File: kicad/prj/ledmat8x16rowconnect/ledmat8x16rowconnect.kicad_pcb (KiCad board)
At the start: 2 copper layers, 15.9 x 63.8 mm, 2 parts, among them J1 Conn_02x08_Odd_Even, J2 Conn_02x08_Odd_Even

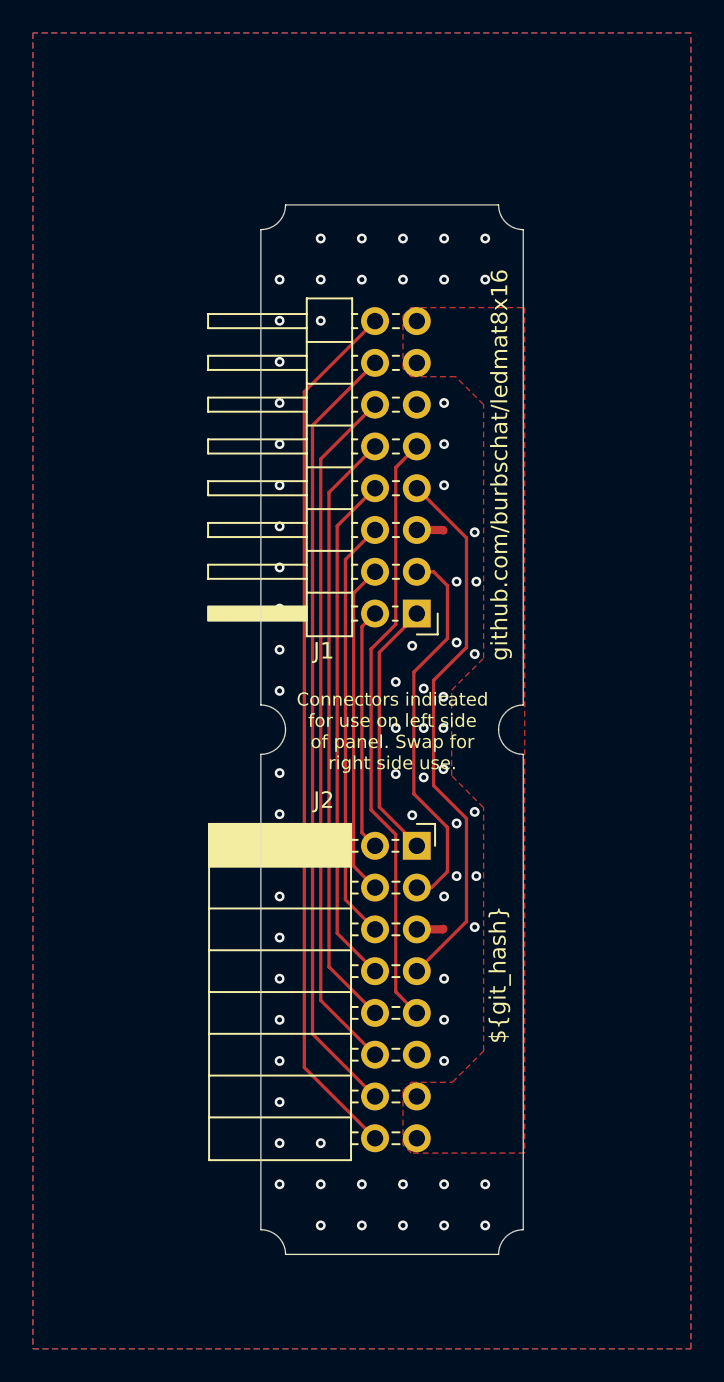
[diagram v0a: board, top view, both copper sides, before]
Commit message: Resize row-connect board to 32mm outline
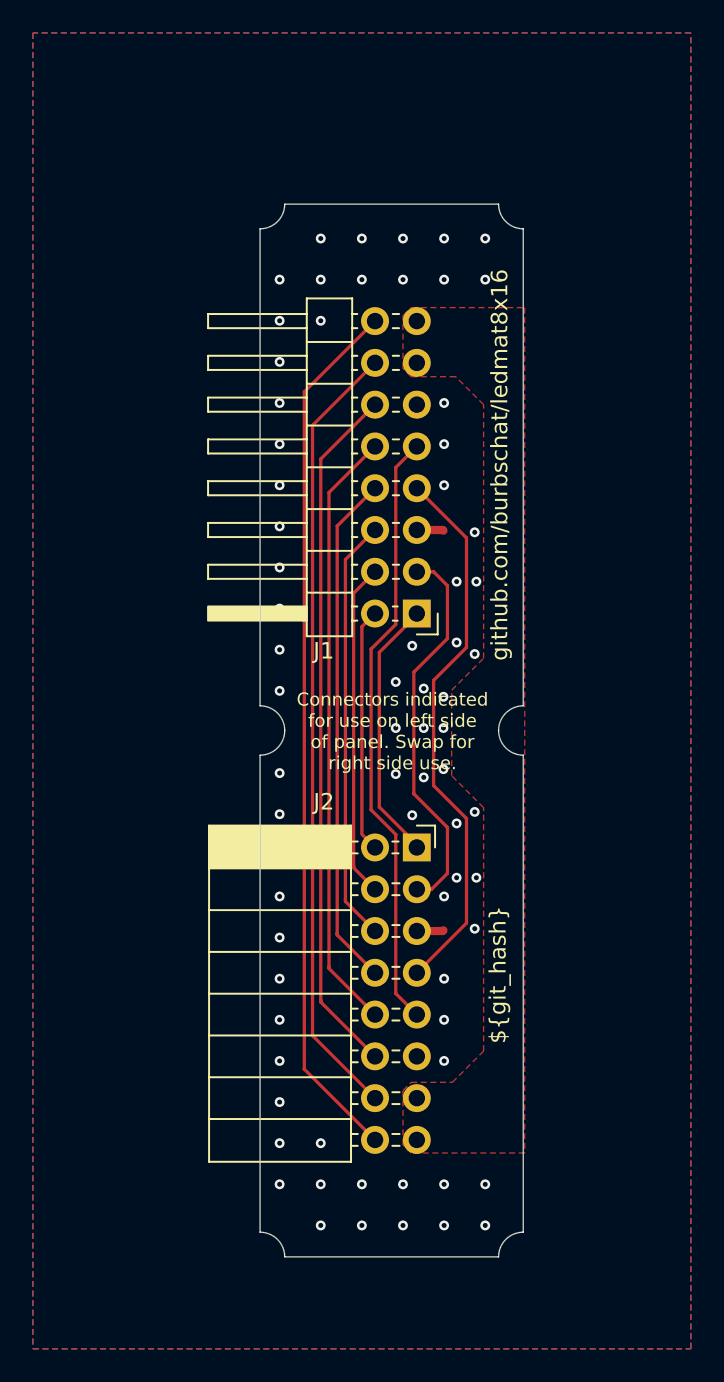
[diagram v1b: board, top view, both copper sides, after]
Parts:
- moved J2 0.10 mm to (138.3, 104.5)
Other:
- board size 15.9 x 63.8 mm -> 16 x 64 mm
